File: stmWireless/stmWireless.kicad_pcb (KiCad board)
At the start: 4 copper layers, 52 parts, among them IC1 BALFLB-WL-02D3, J1 SWD, J2 CORTEX_DEBUG, J3 Power, J5 i2c3 header, J6 GPIO1, U1 STM32WLE5CBU6, U2 AP63203WU, U3 BGS12WN6E6327, Y1 Crystal_32MHz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

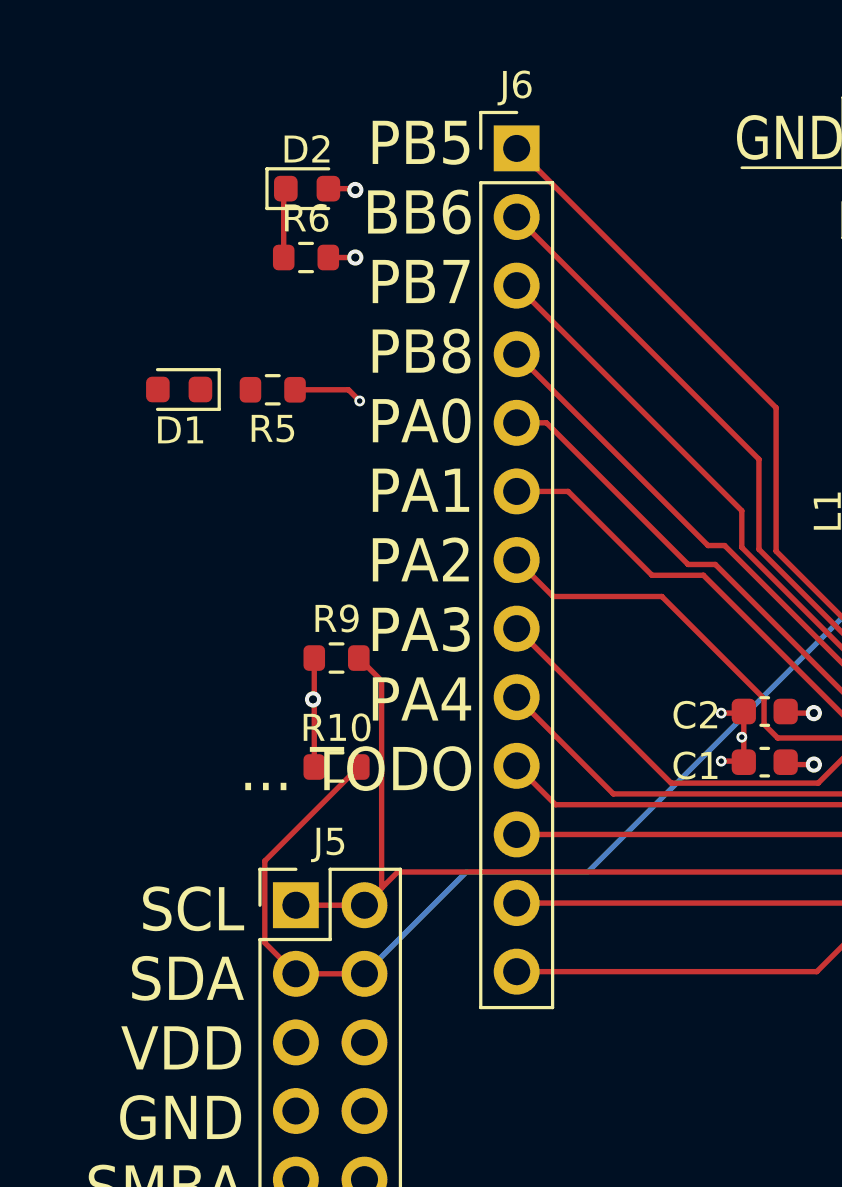
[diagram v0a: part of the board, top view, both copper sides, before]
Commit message: improve highlighted notes on datasheet, and add additional reference about impedance matching networks. Also add pin labels to schematic and PCB GPIO pins
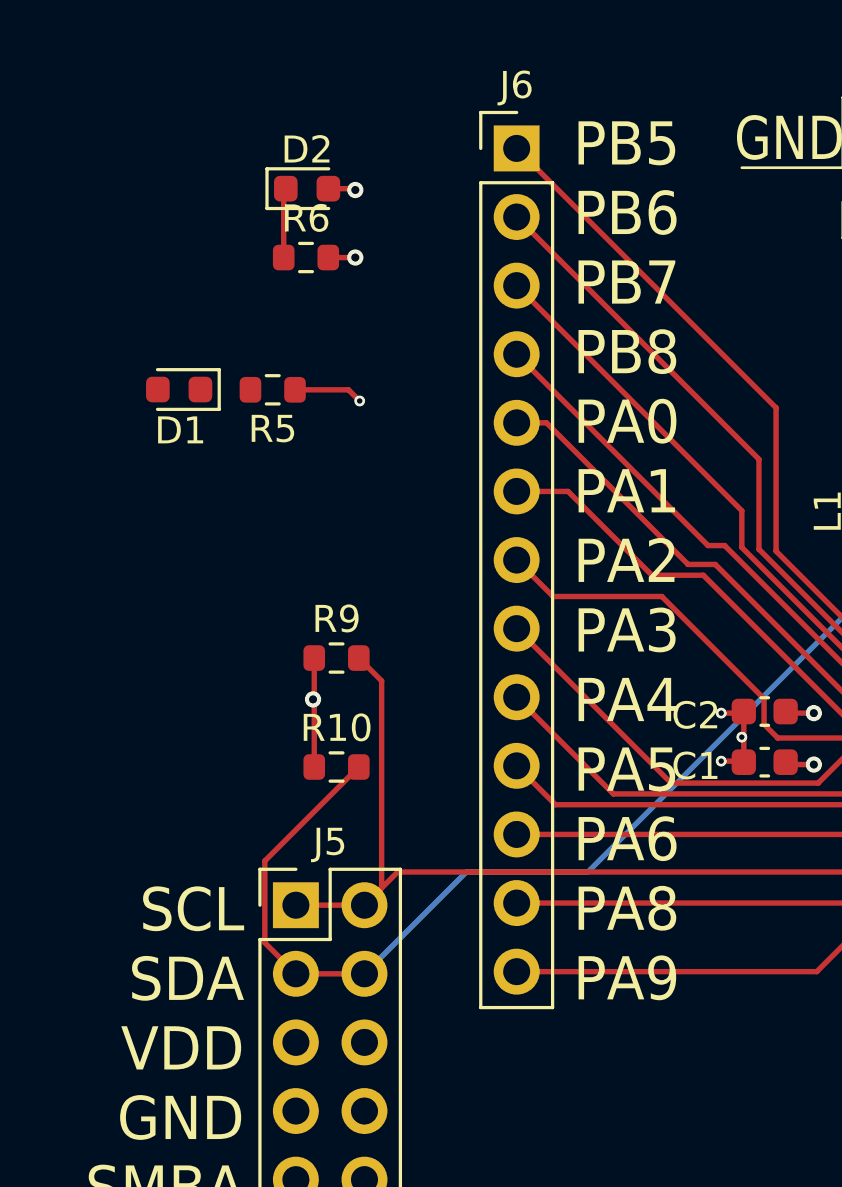
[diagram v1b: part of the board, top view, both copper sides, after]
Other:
- board text added: "PB5 PB6 PB7 PB8 PA0 PA1 PA2 PA3 PA4 PA5 PA6 PA8 PA9"
- board text removed: "PB5 BB6 PB7 PB8 PA0 PA1 PA2 PA3 PA4 ... TODO"
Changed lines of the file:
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@@
 		(layer "Cmts.User")
 	)
-	(gr_text "PB5\nBB6\nPB7\nPB8\nPA0\nPA1\nPA2\nPA3\nPA4\n... TODO"
-		(at 120.904 89.916 0)
+	(gr_text "PB5\nPB6\nPB7\nPB8\nPA0\nPA1\nPA2\nPA3\nPA4\nPA5\nPA6\nPA8\nPA9"
+		(at 128.524 97.663 0)
 		(layer "F.SilkS")
 		(effects

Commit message: initial layout of radio portion, add another reference design with BOM. still need to adjust impedance and add connector
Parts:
- added L3: 47nH, Inductor_SMD:L_0603_1608Metric, F.Cu at (143.1, 94.4)
- added L4: 0R, Inductor_SMD:L_0603_1608Metric, F.Cu at (146.6, 105.9)
- moved C26 12.3 mm to (147.3, 98.3), turned to -90 degrees
- moved C16 11.2 mm to (147.4, 94.9), turned to -90 degrees
- moved IC1 9.50 mm to (139.9, 97.3), turned to -90 degrees
- moved C18 8.84 mm to (142.6, 97.0), turned to -90 degrees
- moved R8 8.80 mm to (153.2, 98.2), turned to 90 degrees
- moved C15 8.71 mm to (145.5, 94.9), turned to -90 degrees
- moved C17 8.59 mm to (140.7, 93.6), turned to 90 degrees
- moved C20 7.80 mm to (140.3, 101.8)
- moved R7 6.70 mm to (140.2, 103.5), turned to 180 degrees
- moved C19 6.40 mm to (135.0, 100.2), turned to 90 degrees
- moved U3 5.93 mm to (143.0, 99.6), turned to -90 degrees
- moved C27 5.65 mm to (150.2, 98.2), turned to -90 degrees
- moved C22 5.18 mm to (143.9, 103.0), turned to 180 degrees
- moved C21 3.95 mm to (140.2, 100.1)
- moved C24 3.31 mm to (144.0, 104.9)
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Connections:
- net Net-(IC1-RFI_N_OUT) renamed Net-IC1-RFI_N
- net Net-(IC1-RFI_P_OUT) renamed Net-IC1-RFI_P
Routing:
- net GND: track 37.4 -> 62.0 mm, vias 41 -> 47
- net RF-CTRL: track 0.00 -> 22.0 mm, vias 0 -> 2
- net /NRST: track 26.1 -> 41.9 mm
- net Net-(U3-CTRL): track 0.00 -> 10.1 mm
- net Net-(IC1-RFI_IN): track 0.00 -> 8.73 mm
- net Net-(U1-VR_PA): track 0.00 -> 8.42 mm
- net Net-IC1-RFI_P: track 0.00 -> 7.63 mm
- net Net-IC1-RFI_N: track 0.00 -> 7.63 mm
- net Net-(U1-RFO_HP): track 0.00 -> 6.02 mm
- net Net-(U3-VDD): track 0.00 -> 5.08 mm
- net Net-(C22-Pad1): track 0.00 -> 3.83 mm
- net Net-(U3-RFIN): track 0.00 -> 3.29 mm
- net Net-(IC1-RFO_OUT): track 0.00 -> 3.08 mm
- net Net-(IC1-RFO_IN): track 0.00 -> 2.91 mm
- net Net-(U3-RF2): track 0.00 -> 1.92 mm
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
